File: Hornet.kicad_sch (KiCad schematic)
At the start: 7 parts, among them J1 Conn_01x04_Female, U1 AP63203WU

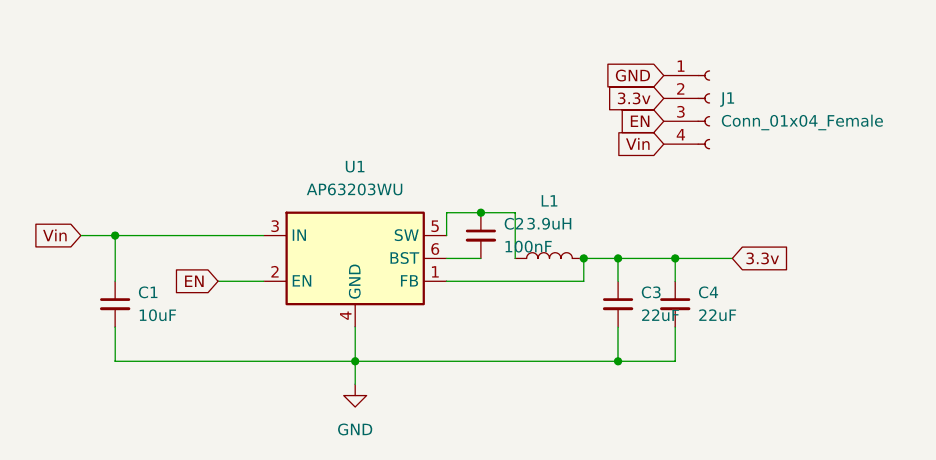
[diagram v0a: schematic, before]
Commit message: Second layout to make board smaller
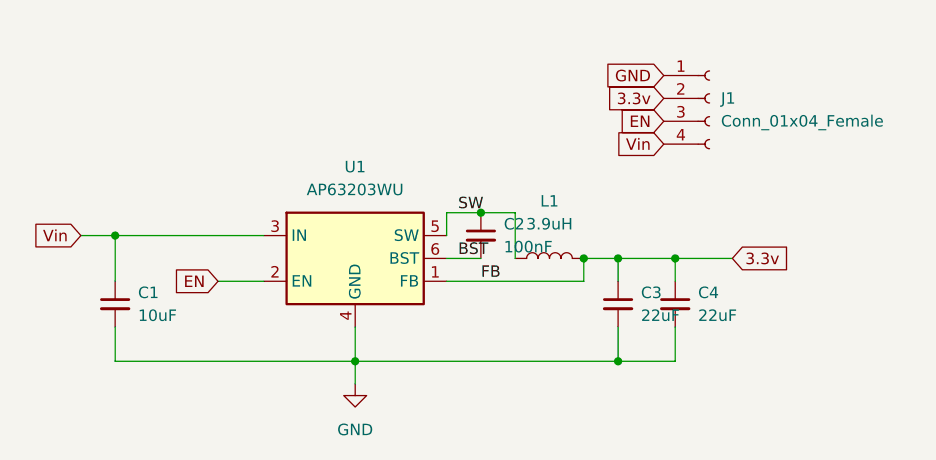
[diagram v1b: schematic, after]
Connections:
- net SW: now reaches C2.1, L1.1, U1.5 (SW)
- net BST: now reaches C2.2, U1.6 (BST)
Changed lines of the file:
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@@
     (stroke (width 0) (type default) (color 0 0 0 0))
+  )
+  (label "FB" (at 158.75 87.63 0)
+    (effects (font (size 1.27 1.27)) (justify left bottom))
+  )
+  (label "SW" (at 156.21 80.01 0)
+    (effects (font (size 1.27 1.27)) (justify left bottom))
+  )
+  (label "BST" (at 156.21 85.09 0)
+    (effects (font (size 1.27 1.27)) (justify left bottom))
   )
   (global_label "3.3v" (shape input) (at 179.07 67.31 180) (fields_autoplaced)

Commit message: New layout and added component part numbers
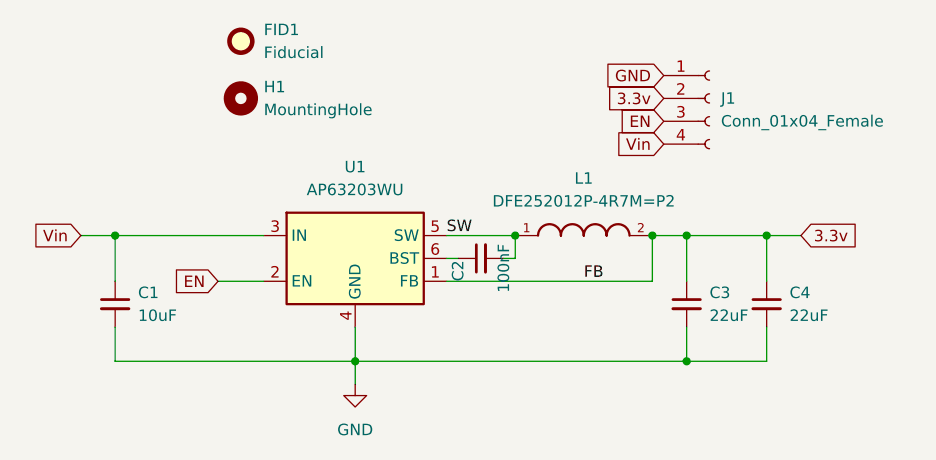
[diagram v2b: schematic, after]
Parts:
- removed L1: 3.9uH, Inductor_SMD:L_Bourns-SRN6028, symbol Device:L
- added FID1: Fiducial, Fiducial:Fiducial_0.5mm_Mask1.5mm, symbol Mechanical:Fiducial
- added H1: MountingHole, MountingHole:MountingHole_3.2mm_M3_ISO7380, symbol Mechanical:MountingHole
- added L1: DFE252012P-4R7M=P2, INDC2520X120N, symbol SnapEDA-library:DFE252012P-4R7M=P2
- C1: footprint Capacitor_SMD:C_0603_1608Metric -> Capacitor_SMD:C_0805_2012Metric
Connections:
- net 3.3v: now also L1.2
- net SW: now also C2.2, L1.1; no longer C2.1
- net BST: no longer names the net of U1.6 (BST)
- net BST: now also C2.1; no longer C2.2
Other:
- moved on the sheet: C2, C3, C4
